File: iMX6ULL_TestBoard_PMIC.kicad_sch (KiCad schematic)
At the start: 44 parts, among them SW1 SW_Push, U1 MC32PF1550A6EP

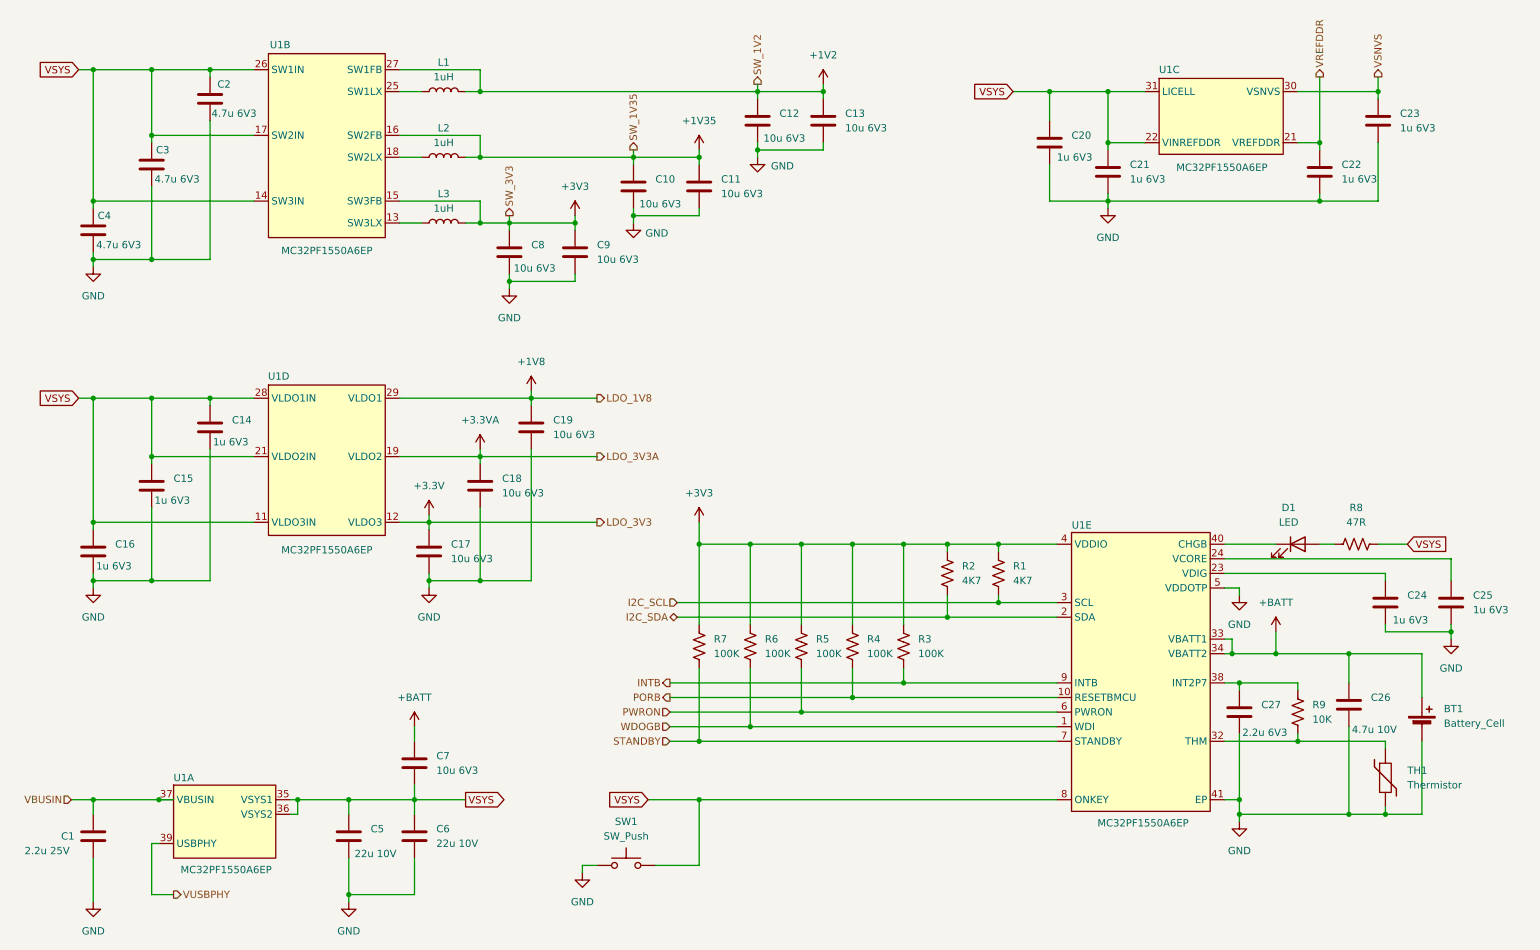
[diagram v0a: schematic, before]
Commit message: Added IMX6ULL Power, Control and DDR sheets. Added symbol library with used custom components.
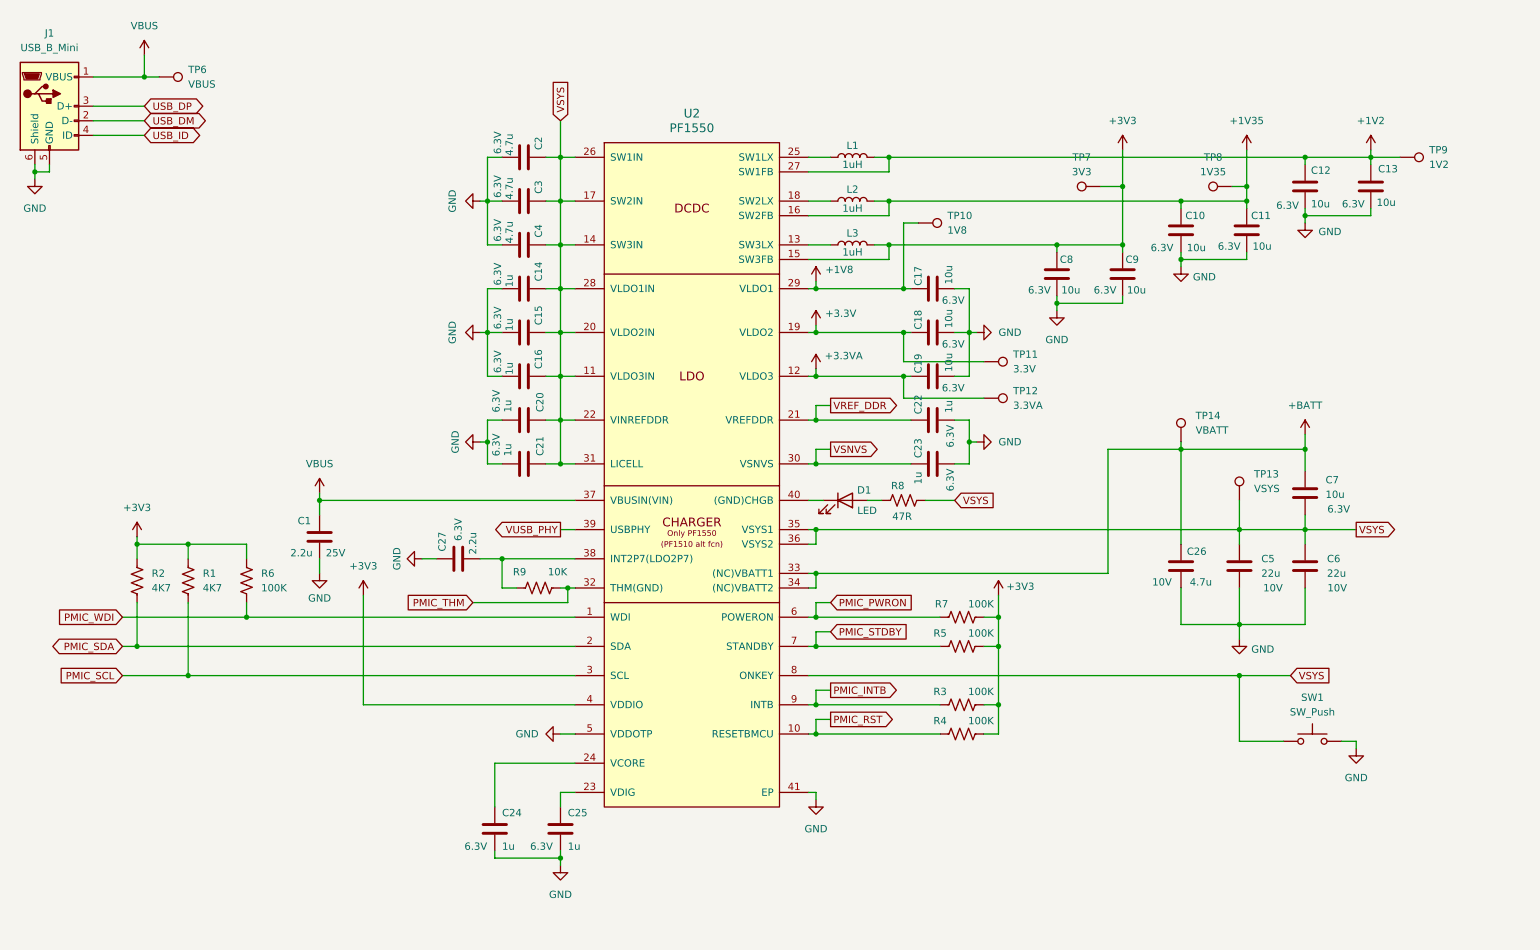
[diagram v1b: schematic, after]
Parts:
- removed BT1: Battery_Cell, symbol Device:Battery_Cell
- removed TH1: Thermistor, symbol Device:Thermistor
- removed U1: MC32PF1550A6EP, symbol AO_Regulator_Switching:PF1550
- added J1: USB_B_Mini, symbol Connector:USB_B_Mini
- added TP10: 1V8, symbol Connector:TestPoint
- added TP11: 3.3V, symbol Connector:TestPoint
- added TP12: 3.3VA, symbol Connector:TestPoint
- added TP13: VSYS, symbol Connector:TestPoint
- added TP14: VBATT, symbol Connector:TestPoint
- added TP6: VBUS, symbol Connector:TestPoint
- added TP7: 3V3, symbol Connector:TestPoint
- added TP8: 1V35, symbol Connector:TestPoint
- added TP9: 1V2, symbol Connector:TestPoint
- added U2: PF1550, symbol iMX6ULL_TestBoard:PF1550
- C1: value 2.2u 25V -> 2.2u; Voltaje (none) -> 25V
- C10, C11, C12, C13, C17, C18, C19, C7, C8, C9: value 10u 6V3 -> 10u; Voltaje (none) -> 6.3V
- C14, C15, C16, C20, C21, C22, C23, C24, C25: value 1u 6V3 -> 1u; Voltaje (none) -> 6.3V
- C2, C3, C4: value 4.7u 6V3 -> 4.7u; Voltaje (none) -> 6.3V
- C26: value 4.7u 10V -> 4.7u; Voltaje (none) -> 10V
- C27: value 2.2u 6V3 -> 2.2u; Voltaje (none) -> 6.3V
- C5, C6: value 22u 10V -> 22u; Voltaje (none) -> 10V
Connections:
- net INTB is gone; now on net +3V3: R3.2
- net PORB is gone; now on net +3V3: R4.2
- net PWRON is gone; now on net +3V3: R5.2
- net STANDBY is gone; now on net +3V3: R7.2
- net +1V2: now also TP9.1, U2.27 (SW1FB)
- net +1V35: now also TP8.1, U2.16 (SW2FB)
- net +1V8: now also C17.1, TP10.1, U2.29 (VLDO1); no longer C19.1
- net +3.3V: now also C18.1, TP11.1, U2.19 (VLDO2); no longer C17.1
- net +3.3VA: now also C19.1, TP12.1, U2.12 (VLDO3); no longer C18.1
- net +3V3: now also TP7.1, U2.15 (SW3FB), U2.4 (VDDIO); no longer R3.1, R4.1, R5.1, R7.1
- net +BATT: now also TP14.1, U2.33 ((NC)VBATT1), U2.34 ((NC)VBATT2)
- net GND: now also C27.1, J1.5 (GND), J1.6 (Shield), U2.41 (EP), U2.5 (VDDOTP); no longer C27.2
- net VSNVS: now also U2.30 (VSNVS)
- net VSYS: now also TP13.1, U2.11 (VLDO3IN), U2.14 (SW3IN), U2.17 (SW2IN), U2.20 (VLDO2IN), U2.22 (VINREFDDR), U2.26 (SW1IN), U2.28 (VLDO1IN), U2.31 (LICELL), U2.35 (VSYS1), U2.36 (VSYS2), U2.8 (ONKEY)
- net at L1.1: now also U2.25 (SW1LX)
- net PMIC_THM: now reaches R9.1
- net PMIC_THM: now also U2.32 (THM(GND)); no longer C27.1
- net at R9.2: now also C27.2, U2.38 (INT2P7(LDO2P7))
- net at C24.1: now also U2.24 (VCORE)
- net at L3.1: now also U2.13 (SW3LX)
- net at D1.1 (K): now also U2.40 ((GND)CHGB)
- net at L2.1: now also U2.18 (SW2LX)
- net at C25.1: now also U2.23 (VDIG)
- net I2C_SCL renamed PMIC_SCL
- net PMIC_SCL: now also U2.3 (SCL)
- net I2C_SDA renamed PMIC_SDA
- net PMIC_SDA: now also U2.2 (SDA)
- net VBUSIN renamed VBUS
- net VBUS: now also J1.1 (VBUS), TP6.1, U2.37 (VBUSIN(VIN))
- net VREFDDR renamed VREF_DDR
- net VREF_DDR: now also U2.21 (VREFDDR)
- net WDOGB renamed PMIC_WDI
- net PMIC_WDI: now also U2.1 (WDI)
- new net PMIC_INTB: R3.1, U2.9 (INTB)
- new net PMIC_PWRON: R7.1, U2.6 (POWERON)
- new net PMIC_RST: R4.1, U2.10 (RESETBMCU)
- new net PMIC_STDBY: R5.1, U2.7 (STANDBY)
- new net USB_DM: J1.2 (D-)
- new net USB_DP: J1.3 (D+)
- new net USB_ID: J1.4 (ID)
- new net VUSB_PHY: U2.39 (USBPHY)
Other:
- moved on the sheet: C1, C10, C11, C12, C13, C2, C20, C22, C24, C25, C26, C27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
